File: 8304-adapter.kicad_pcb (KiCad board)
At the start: 2 copper layers, 17.8 x 33 mm, 3 parts, among them J1 Conn_02x10_Counter_Clockwise, U1 74LS245

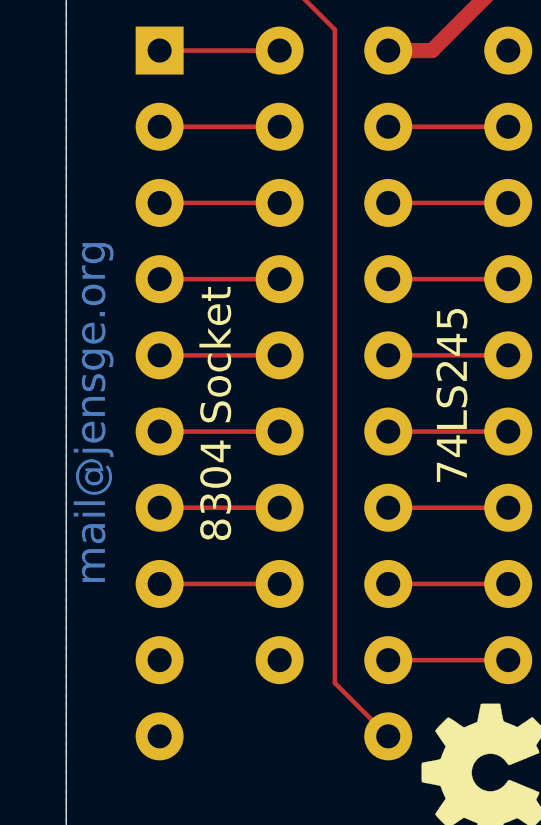
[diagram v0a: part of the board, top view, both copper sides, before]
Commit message: Remove accidental mail address copper
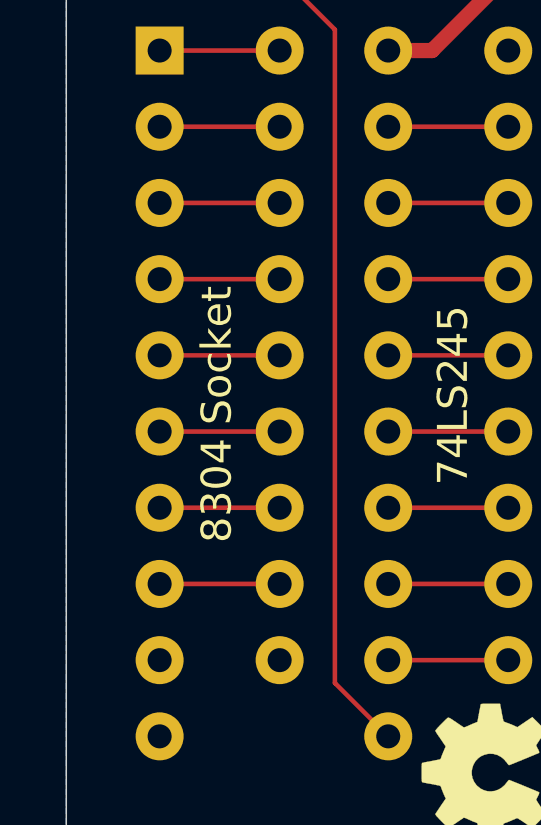
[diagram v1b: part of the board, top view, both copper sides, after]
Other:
- board text removed: "mail@jensge.org"
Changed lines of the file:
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@@
   (general
     (thickness 1.6)
-    (drawings 12)
+    (drawings 11)
     (tracks 21)
     (zones 0)
@@
     (effects (font (size 1 1) (thickness 0.15)))
   )
-  (gr_text mail@jensge.org (at 97.3455 44.069 90) (layer B.Cu)
-    (effects (font (size 1 1) (thickness 0.15)))
-  )

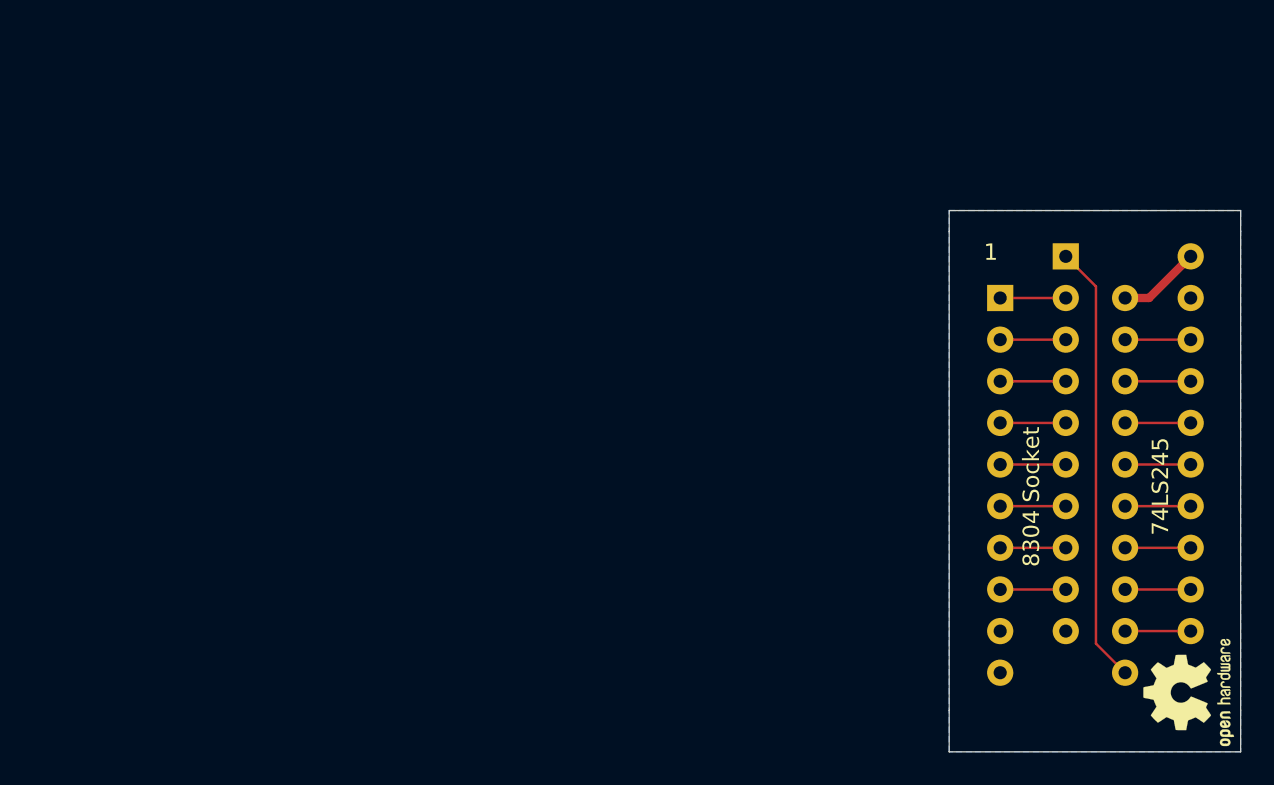
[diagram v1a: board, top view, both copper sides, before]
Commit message: Update layout to use SOIC version of 74LS245
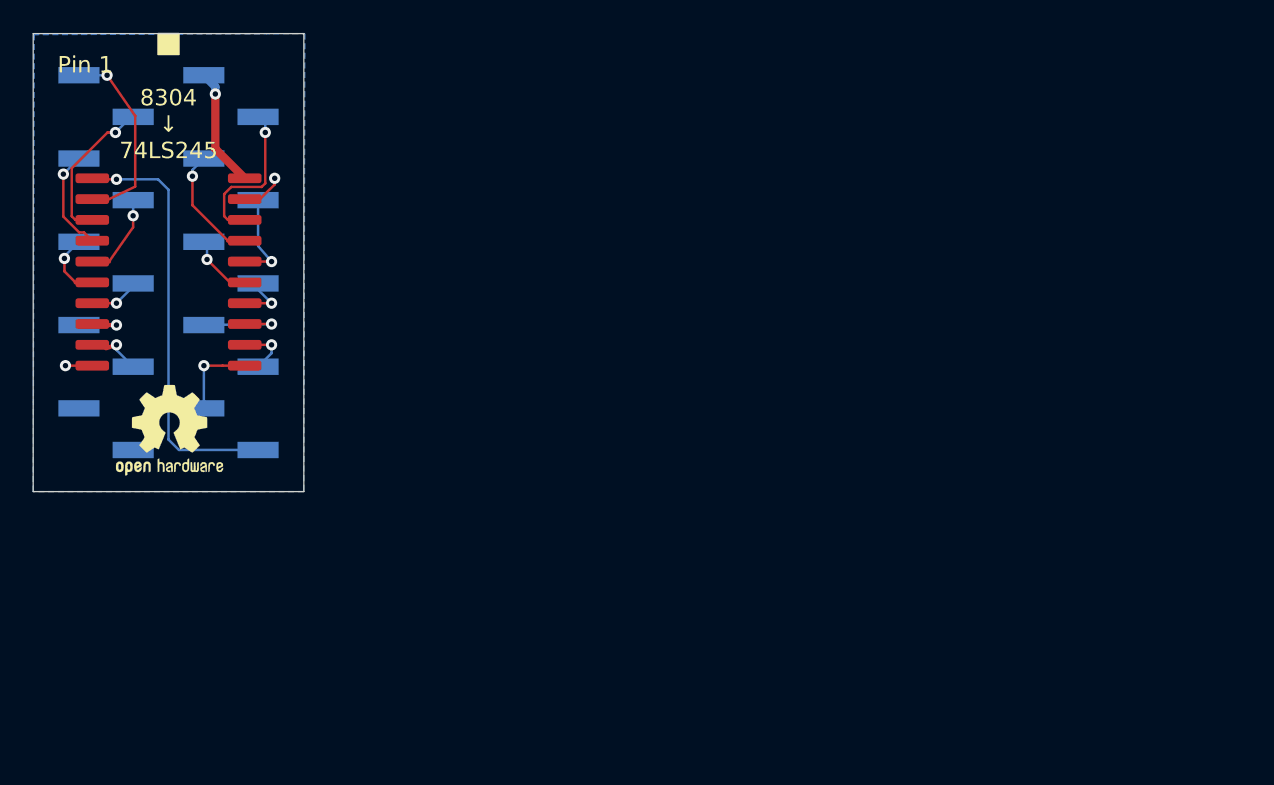
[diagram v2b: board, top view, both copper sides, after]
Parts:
- removed J1: Conn_02x10_Counter_Clockwise, 8304-adapter:DIP-20_W7.62mm-no-slk
- added J2: Conn_01x10, 8304-adapter:PinHeader_1x10_P2.54mm_Vertical_SMD_Pin1Right-nosilk, B.Cu at (45.1, 29.8)
- added J3: Conn_01x10, 8304-adapter:PinHeader_1x10_P2.54mm_Vertical_SMD_Pin1Right-nosilk, B.Cu at (52.7, 29.8)
- U1: footprint 8304-adapter:DIP-20_W7.62mm-no-slk -> 8304-adapter:SOIC-20W_7.5x12.8mm_P1.27mm-nosilk
- moved REF** 64.2 mm to (49.0, 40.1), turned to 0 degrees
- moved U1 54.7 mm to (48.9, 30.4)
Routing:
- net A0: track 4.00 -> 11.8 mm, vias 0 -> 1
- net D0: track 4.00 -> 9.71 mm, vias 0 -> 1
- net A1: track 4.00 -> 9.32 mm, vias 0 -> 1
- net GND: track 0.00 -> 4.21 mm, vias 0 -> 2
- net D1: track 4.00 -> 7.23 mm, vias 0 -> 1
- net +5V: track 5.05 -> 7.32 mm, vias 0 -> 1
- net A2: track 4.00 -> 6.25 mm, vias 0 -> 1
- net D5: track 4.00 -> 5.77 mm, vias 0 -> 1
- net D2: track 4.00 -> 5.69 mm, vias 0 -> 1
- net A7: track 4.00 -> 2.42 mm, vias 0 -> 1
- net A3: track 4.00 -> 5.23 mm, vias 0 -> 1
- net D7: track 4.00 -> 5.09 mm, vias 0 -> 1
- net DIR: track 26.9 -> 25.9 mm, vias 0 -> 1
- net A5: track 4.00 -> 3.10 mm, vias 0 -> 1
- net D4: track 4.00 -> 3.18 mm, vias 0 -> 1
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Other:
- board size 17.8 x 33 mm -> 16.5 x 27.9 mm
- board text added: "8304 ↓ 74LS245"
- board text added: "Pin 1"
- board text removed: "1"
- board text removed: "74LS245"
- board text removed: "8304 Socket"

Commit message: Minor fixes
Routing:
- net A7: track 2.42 -> 3.52 mm
- net A3: track 5.23 -> 4.21 mm
- net A5: track 3.10 -> 3.70 mm
- net A1: track 9.32 -> 9.88 mm
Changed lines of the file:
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@@
     (thickness 1.6)
     (drawings 7)
-    (tracks 110)
+    (tracks 112)
     (zones 0)
     (modules 4)
@@
   (segment (start 45.72 24.765) (end 48.26 24.765) (width 0.1524) (layer B.Cu) (net 2))
   (via (at 45.72 24.765) (size 0.6858) (drill 0.3302) (layers F.Cu B.Cu) (net 2))
-  (segment (start 46.74 20.955) (end 46.609 20.955) (width 0.1524) (layer B.Cu) (net 3))
-  (segment (start 46.609 20.955) (end 45.6565 21.9075) (width 0.1524) (layer B.Cu) (net 3))
   (segment (start 45.6565 21.9075) (end 45.6565 21.9075) (width 0.1524) (layer B.Cu) (net 3))
   (via (at 45.6565 21.9075) (size 0.6858) (drill 0.3302) (layers F.Cu B.Cu) (net 3))
@@
   (segment (start 45.171567 21.9075) (end 42.99139 24.087677) (width 0.1524) (layer F.Cu) (net 3))
   (segment (start 45.6565 21.9075) (end 45.171567 21.9075) (width 0.1524) (layer F.Cu) (net 3))
+  (segment (start 45.6565 20.955) (end 45.6565 21.9075) (width 0.1524) (layer B.Cu) (net 3))
+  (segment (start 46.74 20.955) (end 45.6565 20.955) (width 0.1524) (layer B.Cu) (net 3))
   (segment (start 51.054 36.1315) (end 51.05 38.735) (width 0.1524) (layer B.Cu) (net 4))
   (via (at 51.054 36.1315) (size 0.6858) (drill 0.3302) (layers F.Cu B.Cu) (net 4))
@@
   (segment (start 44.245 28.5115) (end 43.736999 28.003499) (width 0.1524) (layer F.Cu) (net 5))
   (segment (start 42.4815 27.038436) (end 42.4815 24.511) (width 0.1524) (layer F.Cu) (net 5))
-  (segment (start 42.4815 24.4435) (end 43.43 23.495) (width 0.1524) (layer B.Cu) (net 5))
   (segment (start 42.4815 24.4475) (end 42.4815 24.4435) (width 0.1524) (layer B.Cu) (net 5))
+  (segment (start 42.799 23.495) (end 42.4815 23.8125) (width 0.1524) (layer B.Cu) (net 5))
+  (segment (start 43.43 23.495) (end 42.799 23.495) (width 0.1524) (layer B.Cu) (net 5))
+  (segment (start 42.4815 23.8125) (end 42.4815 23.749) (width 0.1524) (layer B.Cu) (net 5))
+  (segment (start 42.4815 24.4435) (end 42.4815 23.8125) (width 0.1524) (layer B.Cu) (net 5))
   (segment (start 53.9115 34.8615) (end 53.545 34.8615) (width 0.254) (layer F.Cu) (net 6))
   (segment (start 55.1815 34.8615) (end 53.9115 34.8615) (width 0.1524) (layer F.Cu) (net 6))
   (via (at 55.1815 34.8615) (size 0.6858) (drill 0.3302) (layers F.Cu B.Cu) (net 6))
-  (segment (start 55.1815 35.3735) (end 54.36 36.195) (width 0.1524) (layer B.Cu) (net 6))
-  (segment (start 55.1815 34.8615) (end 55.1815 35.3735) (width 0.1524) (layer B.Cu) (net 6))
-  (segment (start 45.27 29.7815) (end 44.245 29.7815) (width 0.254) (layer F.Cu) (net 7))
+  (segment (start 55.1815 35.8775) (end 54.36 36.195) (width 0.1524) (layer B.Cu) (net 6))
+  (segment (start 55.1815 34.8615) (end 55.1815 35.8775) (width 0.1524) (layer B.Cu) (net 6))
   (segment (start 46.74 26.3565) (end 46.74 26.035) (width 0.1524) (layer B.Cu) (net 7))
   (segment (start 46.736 26.9875) (end 46.74 26.3565) (width 0.1524) (layer B.Cu) (net 7))
@@
   (segment (start 42.545 29.591) (end 42.545 30.3765) (width 0.1524) (layer F.Cu) (net 9))
   (via (at 42.545 29.591) (size 0.6858) (drill 0.3302) (layers F.Cu B.Cu) (net 9))
-  (segment (start 42.545 29.46) (end 43.43 28.575) (width 0.1524) (layer B.Cu) (net 9))
-  (segment (start 42.545 29.591) (end 42.545 29.46) (width 0.1524) (layer B.Cu) (net 9))
+  (segment (start 42.545 28.956) (end 43.43 28.575) (width 0.1524) (layer B.Cu) (net 9))
+  (segment (start 42.545 29.591) (end 42.545 28.956) (width 0.1524) (layer B.Cu) (net 9))
   (segment (start 53.975 32.3215) (end 53.545 32.3215) (width 0.254) (layer F.Cu) (net 10))
   (segment (start 55.1815 32.3215) (end 53.975 32.3215) (width 0.1524) (layer F.Cu) (net 10))
   (via (at 55.1815 32.3215) (size 0.6858) (drill 0.3302) (layers F.Cu B.Cu) (net 10))
-  (segment (start 54.36 31.5) (end 54.36 31.115) (width 0.1524) (layer B.Cu) (net 10))
-  (segment (start 55.1815 32.3215) (end 54.36 31.5) (width 0.1524) (layer B.Cu) (net 10))
+  (segment (start 55.1815 31.4325) (end 54.36 31.115) (width 0.1524) (layer B.Cu) (net 10))
+  (segment (start 55.1815 32.3215) (end 55.1815 31.4325) (width 0.1524) (layer B.Cu) (net 10))
   (segment (start 44.245 32.3215) (end 45.72 32.3215) (width 0.1524) (layer F.Cu) (net 11))
   (segment (start 45.72 32.3215) (end 45.72 32.3215) (width 0.1524) (layer F.Cu) (net 11))
   (via (at 45.72 32.3215) (size 0.6858) (drill 0.3302) (layers F.Cu B.Cu) (net 11))
-  (segment (start 46.74 31.3015) (end 46.74 31.115) (width 0.1524) (layer B.Cu) (net 11))
-  (segment (start 45.72 32.3215) (end 46.74 31.3015) (width 0.1524) (layer B.Cu) (net 11))
+  (segment (start 45.72 31.115) (end 46.74 31.115) (width 0.1524) (layer B.Cu) (net 11))
+  (segment (start 45.72 32.3215) (end 45.72 31.115) (width 0.1524) (layer B.Cu) (net 11))
   (segment (start 52.6415 31.0515) (end 53.545 31.0515) (width 0.254) (layer F.Cu) (net 12))
   (segment (start 51.2445 29.6545) (end 52.6415 31.0515) (width 0.1524) (layer F.Cu) (net 12))
@@
   (via (at 55.1815 29.7815) (size 0.6858) (drill 0.3302) (layers F.Cu B.Cu) (net 14))
   (segment (start 55.1815 29.7815) (end 53.545 29.7815) (width 0.1524) (layer F.Cu) (net 14))
-  (segment (start 45.724 35.179) (end 46.74 36.195) (width 0.1524) (layer B.Cu) (net 15))
-  (segment (start 45.72 34.8615) (end 45.724 35.179) (width 0.1524) (layer B.Cu) (net 15))
-  (segment (start 45.72 34.8615) (end 45.085 35.075067) (width 0.254) (layer F.Cu) (net 15))
   (via (at 45.72 34.8615) (size 0.6858) (drill 0.3302) (layers F.Cu B.Cu) (net 15))
+  (segment (start 45.72 34.8615) (end 44.245 34.8615) (width 0.254) (layer F.Cu) (net 15))
+  (segment (start 45.72 35.814) (end 46.74 36.195) (width 0.1524) (layer B.Cu) (net 15))
+  (segment (start 45.72 34.8615) (end 45.72 35.814) (width 0.1524) (layer B.Cu) (net 15))
   (segment (start 52.52 28.5115) (end 53.545 28.5115) (width 0.254) (layer F.Cu) (net 16))
   (segment (start 50.3555 26.347) (end 52.52 28.5115) (width 0.1524) (layer F.Cu) (net 16))
   (segment (start 50.3555 24.5745) (end 50.3555 26.347) (width 0.1524) (layer F.Cu) (net 16))
   (via (at 50.3555 24.5745) (size 0.6858) (drill 0.3302) (layers F.Cu B.Cu) (net 16))
-  (segment (start 50.3555 24.1895) (end 51.05 23.495) (width 0.1524) (layer B.Cu) (net 16))
-  (segment (start 50.3555 24.5745) (end 50.3555 24.1895) (width 0.1524) (layer B.Cu) (net 16))
+  (segment (start 50.3555 23.495) (end 51.05 23.495) (width 0.1524) (layer B.Cu) (net 16))
+  (segment (start 50.3555 24.5745) (end 50.3555 23.495) (width 0.1524) (layer B.Cu) (net 16))
   (segment (start 52.52 27.2415) (end 53.545 27.2415) (width 0.1524) (layer F.Cu) (net 17))
   (segment (start 52.29139 27.01289) (end 52.52 27.2415) (width 0.1524) (layer F.Cu) (net 17))
@@
   (segment (start 55.372 25.0825) (end 54.462678 25.9715) (width 0.1524) (layer F.Cu) (net 18))
   (segment (start 55.372 24.7015) (end 55.372 25.0825) (width 0.1524) (layer F.Cu) (net 18))
-  (segment (start 51.7525 19.1175) (end 51.05 18.415) (width 0.508) (layer B.Cu) (net 19))
-  (segment (start 51.7525 19.558) (end 51.7525 19.1175) (width 0.508) (layer B.Cu) (net 19))
   (segment (start 51.7525 22.909) (end 53.545 24.7015) (width 0.508) (layer F.Cu) (net 19))
   (segment (start 51.7525 19.558) (end 51.7525 22.909) (width 0.508) (layer F.Cu) (net 19))
   (via (at 51.7525 19.558) (size 0.6858) (drill 0.3302) (layers F.Cu B.Cu) (net 19))
+  (segment (start 51.7525 18.7325) (end 51.05 18.415) (width 0.508) (layer B.Cu) (net 19))
+  (segment (start 51.7525 19.558) (end 51.7525 18.7325) (width 0.508) (layer B.Cu) (net 19))
   (zone (net 18) (net_name GND) (layer B.Cu) (hatch edge 0.508)
     (connect_pads (clearance 0.508))
